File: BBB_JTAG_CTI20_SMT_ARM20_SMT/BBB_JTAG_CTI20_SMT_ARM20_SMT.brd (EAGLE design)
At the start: 14 x 38 mm, 3 parts, among them P1 CTI20 JTAG, P2 ARM20 JTAG

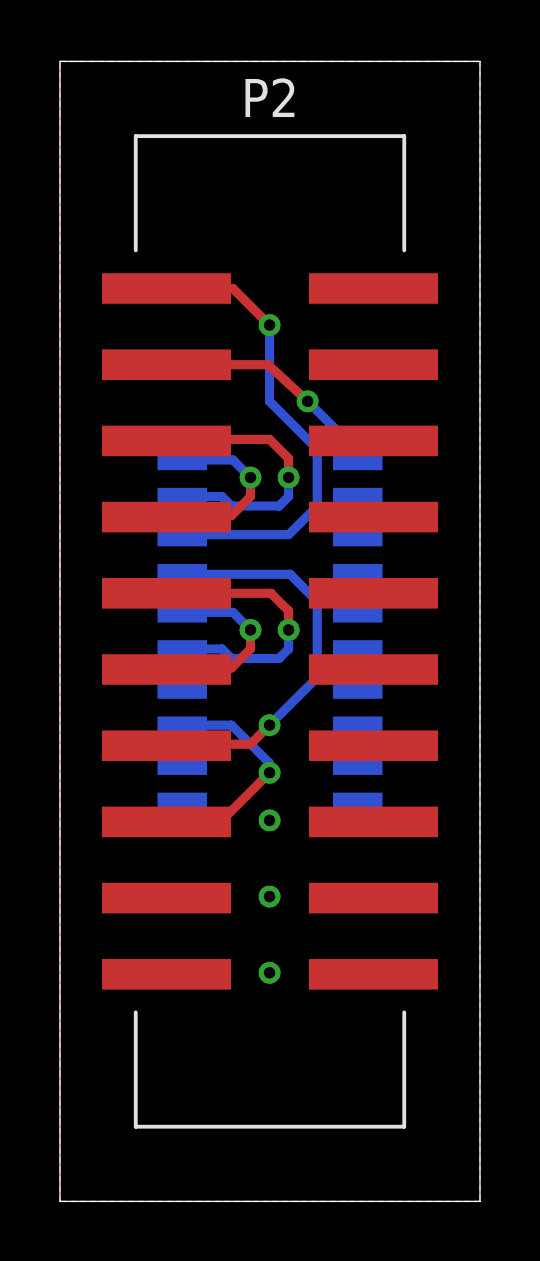
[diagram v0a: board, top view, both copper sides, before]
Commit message: Reroute to make P1 silkscreen fully visible
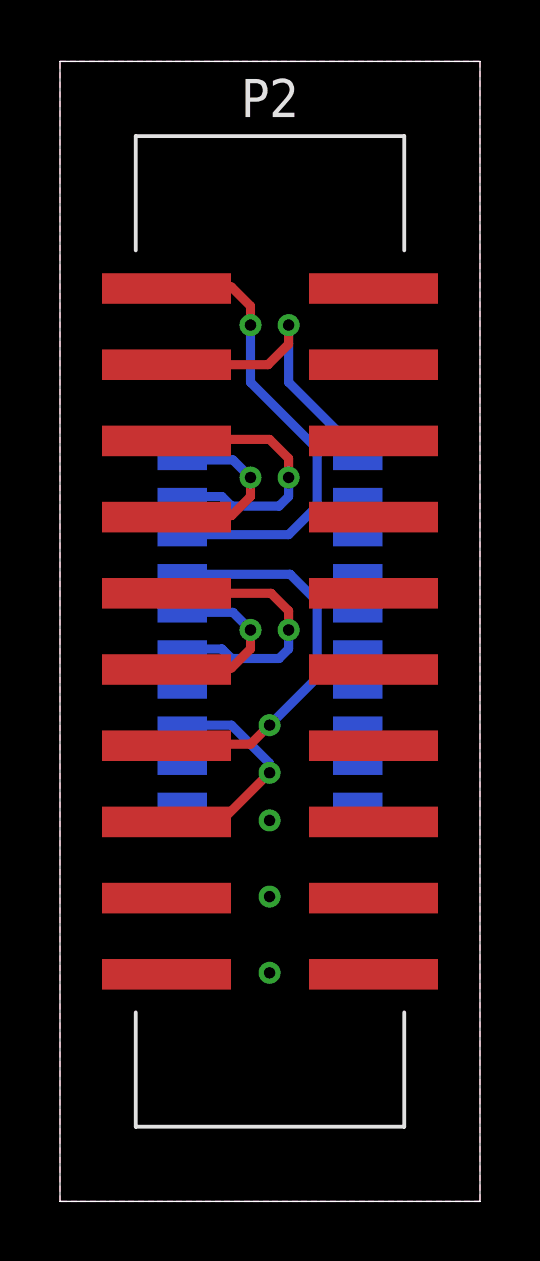
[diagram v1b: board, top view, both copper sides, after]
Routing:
- net TRST_N: track 8.13 -> 10.5 mm
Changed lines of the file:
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@@
 </class>
 </classes>
-<designrules name="LaenPCBOrder">
+<designrules name="oshpark-2layer">
 <description language="de">&lt;b&gt;EAGLE Design Rules&lt;/b&gt;
 &lt;p&gt;
@@
 <param name="mvStopFrame" value="1"/>
 <param name="mvCreamFrame" value="0"/>
-<param name="mlMinStopFrame" value="3mil"/>
-<param name="mlMaxStopFrame" value="3mil"/>
+<param name="mlMinStopFrame" value="2.5mil"/>
+<param name="mlMaxStopFrame" value="2.5mil"/>
 <param name="mlMinCreamFrame" value="0mil"/>
 <param name="mlMaxCreamFrame" value="0mil"/>
@@
 <contactref element="P1" pad="5"/>
 <contactref element="P2" pad="1"/>
-<wire x1="3.55" y1="30.43" x2="5.765" y2="30.43" width="0.3048" layer="1"/>
-<wire x1="5.765" y1="30.43" x2="6.985" y2="29.21" width="0.3048" layer="1"/>
-<via x="6.985" y="29.21" extent="1-16" drill="0.381"/>
-<wire x1="6.985" y1="29.21" x2="6.985" y2="26.67" width="0.3048" layer="16"/>
-<wire x1="6.985" y1="26.67" x2="8.5725" y2="25.0825" width="0.3048" layer="16"/>
+<via x="6.35" y="29.21" extent="1-16" drill="0.381"/>
 <wire x1="8.5725" y1="25.0825" x2="8.5725" y2="23.1775" width="0.3048" layer="16"/>
 <wire x1="8.5725" y1="23.1775" x2="7.62" y2="22.225" width="0.3048" layer="16"/>
 <wire x1="7.62" y1="22.225" x2="4.125" y2="22.225" width="0.3048" layer="16"/>
 <wire x1="4.125" y1="22.225" x2="4.075" y2="22.175" width="0.3048" layer="16"/>
+<wire x1="8.5725" y1="25.0825" x2="6.35" y2="27.305" width="0.3048" layer="16"/>
+<wire x1="6.35" y1="27.305" x2="6.35" y2="29.21" width="0.3048" layer="16"/>
+<wire x1="6.35" y1="29.21" x2="6.35" y2="29.845" width="0.3048" layer="1"/>
+<wire x1="6.35" y1="29.845" x2="5.715" y2="30.48" width="0.3048" layer="1"/>
+<wire x1="5.715" y1="30.48" x2="3.6" y2="30.48" width="0.3048" layer="1"/>
+<wire x1="3.6" y1="30.48" x2="3.55" y2="30.43" width="0.3048" layer="1"/>
 </signal>
 <signal name="TDO">
@@
 <contactref element="P1" pad="2"/>
 <contactref element="P2" pad="3"/>
+<via x="7.62" y="29.21" extent="1-16" drill="0.381"/>
+<wire x1="9.975" y1="24.765" x2="9.925" y2="24.715" width="0.3048" layer="16"/>
 <wire x1="3.55" y1="27.89" x2="6.935" y2="27.89" width="0.3048" layer="1"/>
-<wire x1="6.935" y1="27.89" x2="8.255" y2="26.67" width="0.3048" layer="1"/>
-<via x="8.255" y="26.67" extent="1-16" drill="0.381"/>
-<wire x1="8.255" y1="26.67" x2="10.16" y2="24.765" width="0.3048" layer="16"/>
-<wire x1="10.16" y1="24.765" x2="9.975" y2="24.765" width="0.3048" layer="16"/>
-<wire x1="9.975" y1="24.765" x2="9.925" y2="24.715" width="0.3048" layer="16"/>
+<wire x1="6.935" y1="27.89" x2="7.62" y2="28.575" width="0.3048" layer="1"/>
+<wire x1="7.62" y1="28.575" x2="7.62" y2="29.21" width="0.3048" layer="1"/>
+<wire x1="9.925" y1="24.715" x2="9.925" y2="25" width="0.3048" layer="16"/>
+<wire x1="9.925" y1="25" x2="7.62" y2="27.305" width="0.3048" layer="16"/>
+<wire x1="7.62" y1="27.305" x2="7.62" y2="29.21" width="0.3048" layer="16"/>
 </signal>
 <signal name="GND">
